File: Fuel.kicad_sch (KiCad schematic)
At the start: 22 parts, among them U4 BM2LC105, U5 BM2LC105

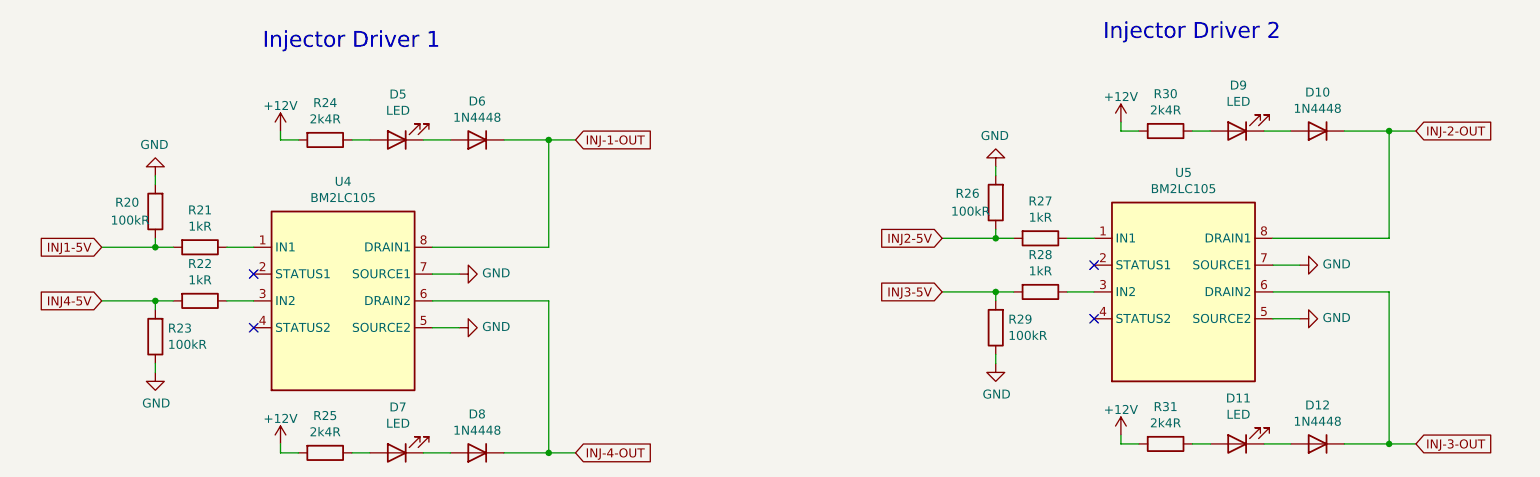
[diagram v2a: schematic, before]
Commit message: Completed layout, slight changes to schematic to optimise routing, 12V proto supply rail removed
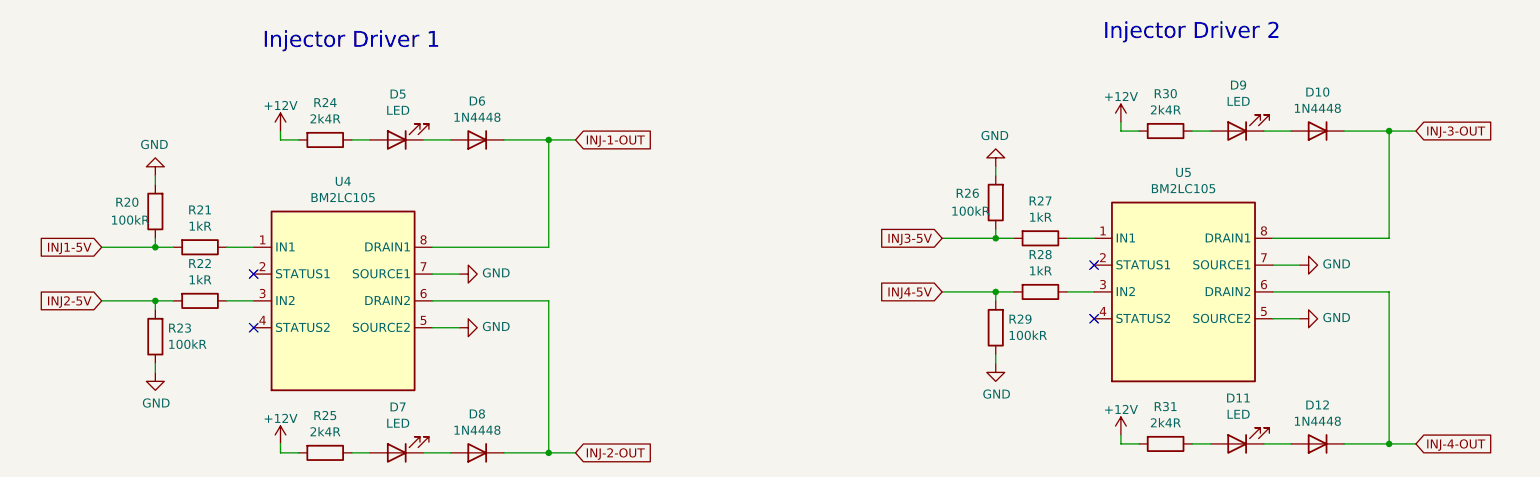
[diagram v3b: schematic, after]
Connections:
- net INJ-2-OUT: now also D8.1 (K), U4.6 (DRAIN2); no longer D10.1 (K), U5.8 (DRAIN1)
- net INJ-3-OUT: now also D10.1 (K), U5.8 (DRAIN1); no longer D12.1 (K), U5.6 (DRAIN2)
- net INJ-4-OUT: now also D12.1 (K), U5.6 (DRAIN2); no longer D8.1 (K), U4.6 (DRAIN2)
- net INJ2-5V: now also R22.2, R23.2; no longer R26.1, R27.2
- net INJ3-5V: now also R26.1, R27.2; no longer R28.2, R29.2
- net INJ4-5V: now also R28.2, R29.2; no longer R22.2, R23.2
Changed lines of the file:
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@@
     (effects (font (size 2.2606 2.2606)) (justify left bottom))
   )
-  (global_label "INJ2-5V" (shape input) (at 173.99 58.42 180) (fields_autoplaced)
+  (global_label "INJ3-5V" (shape input) (at 173.99 58.42 180) (fields_autoplaced)
     (effects (font (size 1.27 1.27)) (justify right))
     (property "Intersheet References" "${INTERSHEET_REFS}" (id 0) (at 163.594 58.3406 0)
@@
     )
   )
-  (global_label "INJ-2-OUT" (shape input) (at 241.3 43.18 0) (fields_autoplaced)
+  (global_label "INJ-3-OUT" (shape input) (at 241.3 43.18 0) (fields_autoplaced)
     (effects (font (size 1.27 1.27)) (justify left))
-    (property "Intersheet References" "${INTERSHEET_REFS}" (id 0) (at 0 0 0)
-      (effects (font (size 1.27 1.27)) hide)
+    (property "Intersheet References" "${INTERSHEET_REFS}" (id 0) (at 254.5988 43.1006 0)
+      (effects (font (size 1.27 1.27)) (justify left) hide)
     )
   )
-  (global_label "INJ-4-OUT" (shape input) (at 121.92 88.9 0) (fields_autoplaced)
+  (global_label "INJ-2-OUT" (shape input) (at 121.92 88.9 0) (fields_autoplaced)
     (effects (font (size 1.27 1.27)) (justify left))
-    (property "Intersheet References" "${INTERSHEET_REFS}" (id 0) (at 0 0 0)
-      (effects (font (size 1.27 1.27)) hide)
+    (property "Intersheet References" "${INTERSHEET_REFS}" (id 0) (at 135.2188 88.8206 0)
+      (effects (font (size 1.27 1.27)) (justify left) hide)
     )
   )
-  (global_label "INJ4-5V" (shape input) (at 54.61 67.31 180) (fields_autoplaced)
+  (global_label "INJ2-5V" (shape input) (at 54.61 67.31 180) (fields_autoplaced)
     (effects (font (size 1.27 1.27)) (justify right))
     (property "Intersheet References" "${INTERSHEET_REFS}" (id 0) (at 44.214 67.2306 0)
@@
     )
   )
-  (global_label "INJ3-5V" (shape input) (at 173.99 66.04 180) (fields_autoplaced)
+  (global_label "INJ4-5V" (shape input) (at 173.99 66.04 180) (fields_autoplaced)
     (effects (font (size 1.27 1.27)) (justify right))
     (property "Intersheet References" "${INTERSHEET_REFS}" (id 0) (at 163.594 65.9606 0)
@@
     )
   )
-  (global_label "INJ-3-OUT" (shape input) (at 241.3 87.63 0) (fields_autoplaced)
+  (global_label "INJ-4-OUT" (shape input) (at 241.3 87.63 0) (fields_autoplaced)
     (effects (font (size 1.27 1.27)) (justify left))
-    (property "Intersheet References" "${INTERSHEET_REFS}" (id 0) (at 0 0 0)
-      (effects (font (size 1.27 1.27)) hide)
+    (property "Intersheet References" "${INTERSHEET_REFS}" (id 0) (at 254.5988 87.5506 0)
+      (effects (font (size 1.27 1.27)) (justify left) hide)
     )
   )
